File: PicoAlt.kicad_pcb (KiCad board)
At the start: 2 copper layers, 21 x 58 mm, 40 parts, among them J2 USB_B, J3 Conn_01x04, J4 Conn_01x20, J5 Conn_01x20, SW1 SW_Push, SW2 SW_Push, U1 AMS1117-3.3, U2 W25Q128JVSIQ, U3 RP2350, Y1 12 MHz

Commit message: rearranged layout
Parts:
- added C6: 4.7 uF, Capacitor_SMD:C_0603_1608Metric, F.Cu at (144.3, 111.2)
- moved R9 15.6 mm to (144.3, 89.7), turned to 0 degrees
- moved R2 2.80 mm to (153.8, 101.6), turned to 180 degrees
- moved C10 2.29 mm to (150.6, 100.4), turned to 0 degrees
- moved L1 0.71 mm to (150.3, 98.7), turned to 180 degrees
- moved C5 0.63 mm to (142.7, 111.2)
- moved C8 0.31 mm to (153.8, 102.6)
- moved C4 0.13 mm to (144.0, 88.4)
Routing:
- net QSPISS: track 32.2 -> 15.2 mm
- net Net-(R9-Pad1): track 64.2 -> 79.9 mm
- net +3.3V: track 113.8 -> 104.0 mm, vias 7 -> 5
- net GND: track 43.6 -> 46.6 mm, vias 40 -> 42
- net ADCVREF: track 15.2 -> 17.6 mm
- net Net-(L1-Pad1): track 1.63 -> 3.61 mm
- net +1V1: track 35.1 -> 37.0 mm, vias 4 -> 6
- net USBM: track 20.5 -> 19.8 mm
- net USBP: track 18.0 -> 17.5 mm
- net Net-(C14-Pad1): track 3.81 -> 3.30 mm

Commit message: Small modifications of placement
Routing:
- net +3.3V: track 104.0 -> 102.9 mm

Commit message: regulator work
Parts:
- added C20: 4.7 uF, Capacitor_SMD:C_0603_1608Metric, F.Cu at (150.6, 100.3)
- moved C4 3.32 mm to (147.3, 88.5)
- moved C15 3.17 mm to (144.1, 89.8), turned to 0 degrees
- moved U2 2.39 mm to (145.1, 94.9), turned to 90 degrees
- moved L1 1.90 mm to (150.4, 96.8)
- moved C10 1.63 mm to (150.6, 98.8)
- moved R9 1.41 mm to (143.8, 88.4), turned to 180 degrees
- moved D2 0.37 mm to (144.4, 83.7)
- moved C18 0.31 mm to (154.0, 96.8)
- moved R7 0.29 mm to (154.0, 98.4)
- moved JP1 0.26 mm to (153.8, 91.6)
- moved U1 0.26 mm to (150.9, 84.1)
- moved R4 0.24 mm to (149.5, 88.8)
- moved R3 0.23 mm to (150.6, 88.8)
- moved C12 0.19 mm to (153.9, 88.9)
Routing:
- net +3.3V: track 102.9 -> 110.0 mm
- net QSPISD1: track 11.6 -> 5.02 mm
- net QSPISD2: track 9.30 -> 4.66 mm
- net GND: track 46.6 -> 50.2 mm, vias 42 -> 43
- net USBP: track 17.5 -> 14.0 mm
- net USBM: track 19.8 -> 16.8 mm
- net +1V1: track 36.7 -> 39.2 mm
- net Net-(L1-Pad1): track 3.61 -> 5.59 mm
- net QSPISD3: track 14.6 -> 16.5 mm
- net QSPICLK: track 13.4 -> 14.9 mm
- net Net-(R9-Pad1): track 79.9 -> 78.5 mm
- net QSPISD0: track 9.53 -> 10.3 mm

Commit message: Changed inductor
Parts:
- L1: footprint Inductor_SMD:L_0805_2012Metric -> PicoAlt:Inductor_SMD_3x3mm
- moved JP1 0.82 mm to (153.8, 90.8)
- moved C12 0.79 mm to (153.9, 88.2)
- moved L1 0.52 mm to (150.2, 96.4), turned to 0 degrees
- moved U1 0.39 mm to (151.0, 83.7)
- moved R7 0.25 mm to (153.9, 98.6)
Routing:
- net GND: track 50.2 -> 52.9 mm, vias 43 -> 44
- net +3.3V: track 110.0 -> 111.2 mm
- net Net-(J5-Pad17): track 6.74 -> 5.93 mm
- net +5V: track 23.1 -> 23.9 mm
- net +1V1: track 39.2 -> 39.8 mm

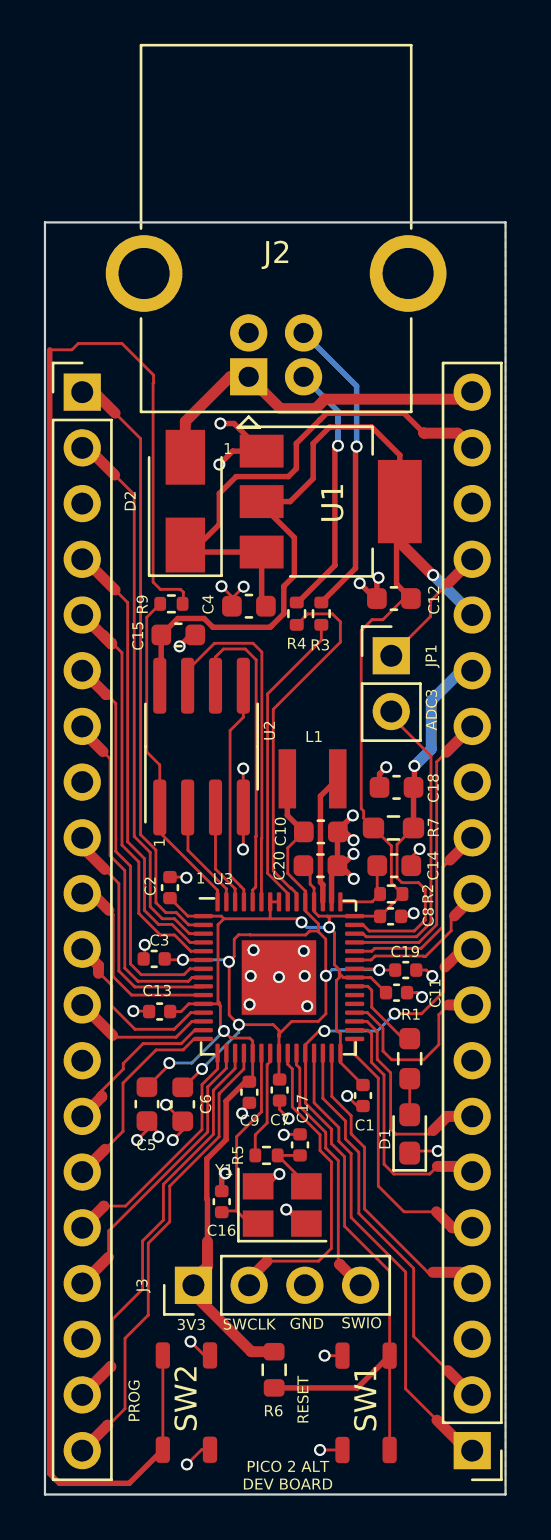
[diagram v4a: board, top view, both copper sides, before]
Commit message: Modified for Abracon inductor and oscillator, sent to JLCPCB
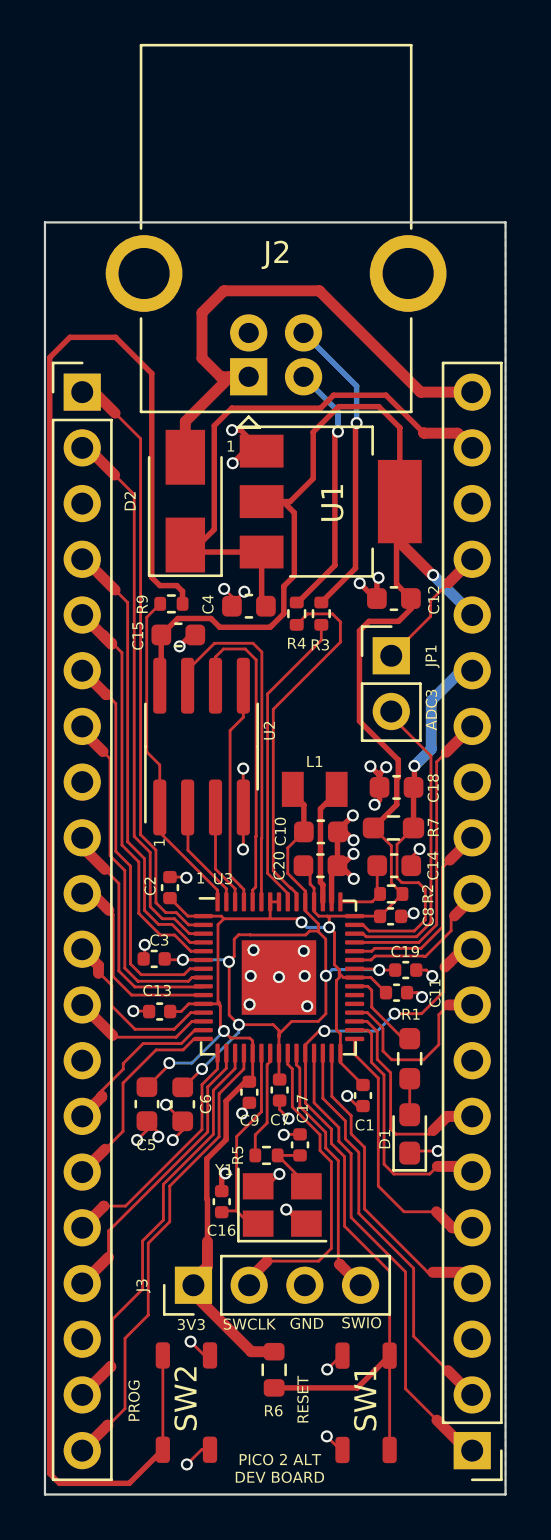
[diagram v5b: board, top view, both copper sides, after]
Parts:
- C16, C17: value 22 pF -> 15 pF
- L1: footprint PicoAlt:Inductor_SMD_3x3mm -> PicoAlt:Abracon_Pico_inductor
- moved L1 0.49 mm to (150.3, 96.8), turned to 180 degrees
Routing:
- net VBUS: track 16.5 -> 24.6 mm
- net +3.3V: track 111.2 -> 114.9 mm
- net +5V: track 23.9 -> 25.8 mm
- net +1V1: track 39.8 -> 39.2 mm
- net Net-(U3-VREG_LX): track 5.98 -> 5.48 mm
- net GND: track 52.9 -> 53.3 mm, vias 44 -> 46
